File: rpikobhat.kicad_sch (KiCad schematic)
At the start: 48 parts, among them J1 Conn_Coaxial_Power, J2 Screw_Terminal_01x02, J3 PI40HAT, J4 Screw_Terminal_01x02, J5 Screw_Terminal_01x02, J6 CONN_02X02, J9 CONN_01X02, Q1 DMG2305UX, Q2 DMMT5401, Q3 IRF640S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

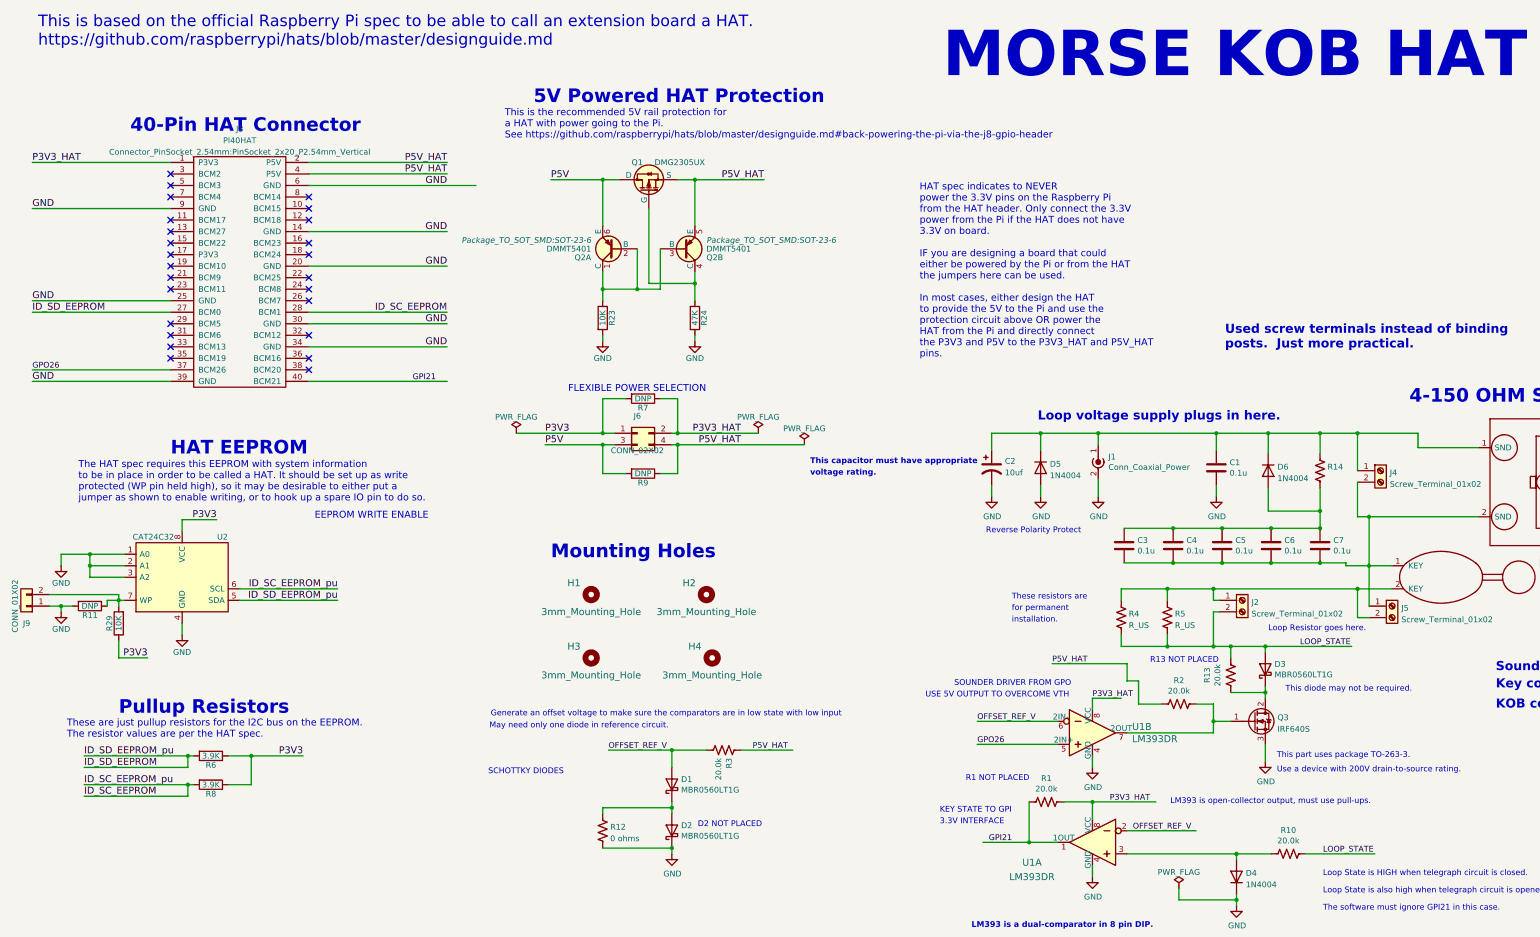
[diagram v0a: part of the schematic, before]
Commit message: Added fan, I2C port, and snubber.  General clean-up.
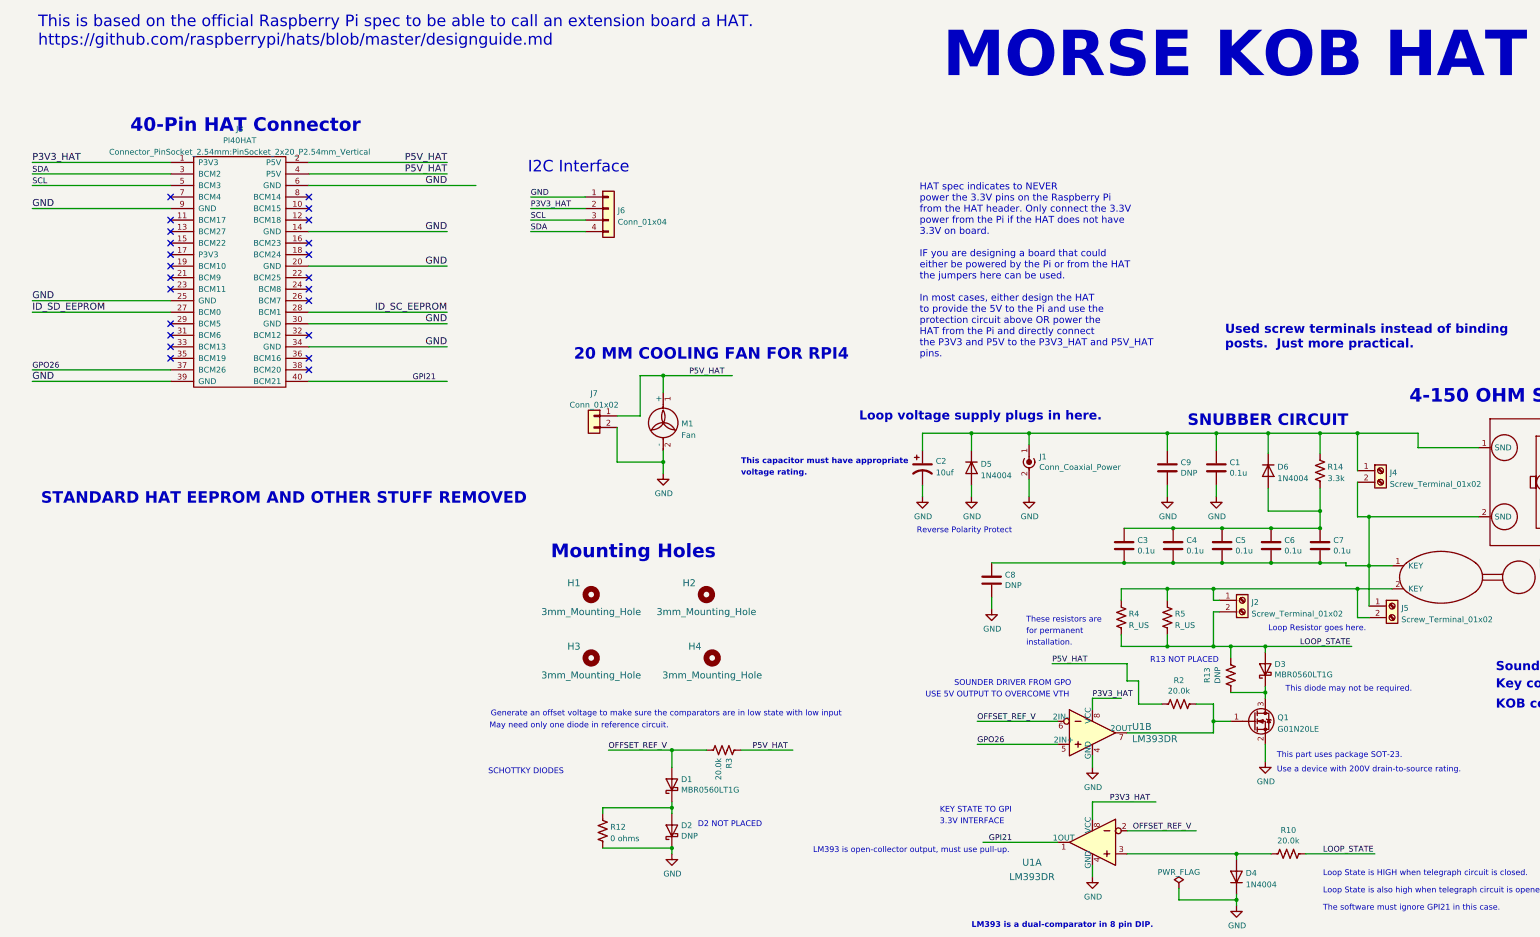
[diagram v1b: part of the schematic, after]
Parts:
- removed J6: CONN_02X02, Connector_PinHeader_2.54mm:PinHeader_2x02_P2.54mm_Vertical, symbol Connector_Generic:Conn_02x02_Odd_Even
- removed J9: CONN_01X02, Connector_PinHeader_2.54mm:PinHeader_1x02_P2.54mm_Vertical, symbol Connector_Generic:Conn_01x02
- removed Q1: DMG2305UX, Package_TO_SOT_SMD:SOT-23, symbol raspberrypi_hat:DMG2305UX
- removed Q2: DMMT5401, Package_TO_SOT_SMD:SOT-23-6, symbol raspberrypi_hat:DMMT5401
- removed Q3: IRF640S, Package_TO_SOT_SMD:TO-263-2, symbol Transistor_FET:IRFS4321
- removed R1: 20.0k, Resistor_SMD:R_1206_3216Metric_Pad1.30x1.75mm_HandSolder, symbol Device:R_US
- removed R11, R7, R9: DNP, Resistor_SMD:R_0603_1608Metric_Pad0.84x1.00mm_HandSolder, symbol Device:R
- removed R23, R29: 10K, Resistor_SMD:R_0603_1608Metric_Pad0.84x1.00mm_HandSolder, symbol Device:R
- removed R24: 47K, Resistor_SMD:R_0603_1608Metric_Pad0.84x1.00mm_HandSolder, symbol Device:R
- removed R6, R8: 3.9K, Resistor_SMD:R_0603_1608Metric_Pad0.84x1.00mm_HandSolder, symbol Device:R
- removed U2: CAT24C32, Package_SOIC:SOIC-8_3.9x4.9mm_P1.27mm, symbol raspberrypi_hat:CAT24C32
- added C8, C9: DNP, Capacitor_SMD:C_1206_3216Metric_Pad1.33x1.80mm_HandSolder, symbol Device:C
- added J6: Conn_01x04, Connector_PinHeader_2.54mm:PinHeader_1x04_P2.54mm_Vertical, symbol Connector_Generic:Conn_01x04
- added J7: Conn_01x02, Connector_PinHeader_2.54mm:PinHeader_1x02_P2.54mm_Vertical, symbol Connector_Generic:Conn_01x02
- added M1: Fan, project_footprints:FAN_20mm, symbol Motor:Fan
- added Q1: G01N20LE, Package_TO_SOT_SMD:SOT-23, symbol Transistor_FET:2N7002
- D2: value MBR0560LT1G -> DNP
- R13: value 20.0k -> DNP
- R14: value (none) -> 3.3k; footprint (none) -> Resistor_SMD:R_1206_3216Metric_Pad1.30x1.75mm_HandSolder
- R4, R5: footprint Resistor_THT:R_Axial_DIN0414_L11.9mm_D4.5mm_P25.40mm_Horizontal -> Resistor_THT:R_Axial_DIN0414_L11.9mm_D4.5mm_P15.24mm_Horizontal
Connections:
- net GND: now also C8.2, C9.2, J6.1 (Pin_1), J7.2 (Pin_2), M1.2 (-), Q1.2 (S)
- net P3V3_HAT: now also J6.2 (Pin_2)
- net P5V_HAT: now also J7.1 (Pin_1), M1.1 (+)
- net at R2.1, U1.7 (2OUT): now also Q1.1 (G)
- net at D3.1 (K), R13.2: now also Q1.3 (D)
- net at C3.2, C4.2, C5.2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: now also C8.1
- net at C1.1, C2.1, D5.1 (K)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: now also C9.1
- net SDA: now reaches J3.3 (BCM2)
- net SDA: now also J6.4 (Pin_4)
- net SCL: now reaches J3.5 (BCM3)
- net SCL: now also J6.3 (Pin_3)
- no-connect marks 25 -> 23
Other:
- note added: "20 MM COOLING FAN FOR RPI4"
- note added: "I2C Interface"
- note added: "LM393 is open-collector output, must use pull-up."
- note added: "SNUBBER CIRCUIT"
- note added: "STANDARD HAT EEPROM AND OTHER STUFF REMOVED"
- note added: "This part uses package SOT-23."
- note removed: "5V Powered HAT Protection"
- note removed: "EEPROM WRITE ENABLE"
- note removed: "FLEXIBLE POWER SELECTION"
- note removed: "HAT EEPROM"
- note removed: "LM393 is open-collector output, must use pull-ups."
- note removed: "Pullup Resistors"
- note removed: "R1 NOT PLACED"
- note removed: "The HAT spec requires this EEPROM with system information to be in place in order to be called a HAT. It should be set up as write protected (WP pin held high), so it may be desirable to either put a jumper as shown to enable writing, or to hook up a spare IO pin to do so."
- note removed: "These are just pullup resistors for the I2C bus on the EEPROM. The resistor values are per the HAT spec."
- note removed: "This is the recommended 5V rail protection for a HAT with power going to the Pi. See https://github.com/raspberrypi/hats/blob/master/designguide.md#back-powering-the-pi-via-the-j8-gpio-header"
- note removed: "This part uses package TO-263-3."
- moved on the sheet: C2, D5, J1
